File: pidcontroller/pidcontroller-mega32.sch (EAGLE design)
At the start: 19 parts, among them IC2 MAX3232CWE, IC3 MEGA32-A

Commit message: more work!
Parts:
- SV3: device con-lstb:MA03-2 -> con-lstb:MA06-1
- renumbered SSR2- to PUMP
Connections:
- removed net LCDCONTR: R3.S, SV1.3
- removed net N$21: IC3.(OC1A)PD5, OW-TMP.P
- new net N$17: R3.S, SV1.2
- net GND: now also IC3.GND, IC3.GND1, IC3.GND2, SV1.1, SV3.5; no longer IC3.VCC2, SV1.2, SV3.6
- net N$10: now also IC3.(OC2)PD7; no longer IC3.(TOSC2)PC7
- net N$14: now also IC3.(MOSI)PB5; no longer IC3.(MISO)PB6
- net N$15: now also IC3.(MISO)PB6, SV3.2; no longer IC3.(MOSI)PB5, SV3.4
- net N$4: now also IC3.(OC1A)PD5; no longer IC3.(TOSC1)PC6
- net RESET: now also SV3.4; no longer SV3.5
- net VCC: now also IC3.AVCC, IC3.VCC1, IC3.VCC2, SV1.3, SV3.6; no longer SV1.1, SV3.2
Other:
- moved on the sheet: OW-TMP, SV3

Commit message: prettified board
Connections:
- net GND: now also SV3.6; no longer SV3.5
- net VCC: now also SV3.5; no longer SV3.6
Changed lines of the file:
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@@
-</segment>
-<segment>
-<pinref part="P+4" gate="VCC" pin="VCC"/>
-<wire x1="99.06" y1="63.5" x2="96.52" y2="63.5" width="0.1524" layer="91"/>
-<pinref part="SV3" gate="1" pin="6"/>
-<wire x1="96.52" y1="63.5" x2="96.52" y2="48.26" width="0.1524" layer="91"/>
-<wire x1="96.52" y1="48.26" x2="104.14" y2="48.26" width="0.1524" layer="91"/>
 </segment>
 <segment>
@@
 <wire x1="96.52" y1="101.6" x2="96.52" y2="88.9" width="0.1524" layer="91"/>
 <wire x1="96.52" y1="88.9" x2="104.14" y2="88.9" width="0.1524" layer="91"/>
+</segment>
+<segment>
+<pinref part="P+4" gate="VCC" pin="VCC"/>
+<pinref part="SV3" gate="1" pin="5"/>
+<wire x1="99.06" y1="63.5" x2="99.06" y2="50.8" width="0.1524" layer="91"/>
+<wire x1="99.06" y1="50.8" x2="104.14" y2="50.8" width="0.1524" layer="91"/>
 </segment>
 </net>
@@
 </segment>
 <segment>
-<pinref part="GND6" gate="1" pin="GND"/>
-<pinref part="SV3" gate="1" pin="5"/>
-<wire x1="99.06" y1="43.18" x2="99.06" y2="50.8" width="0.1524" layer="91"/>
-<wire x1="99.06" y1="50.8" x2="104.14" y2="50.8" width="0.1524" layer="91"/>
-</segment>
-<segment>
 <pinref part="SV1" gate="1" pin="1"/>
 <pinref part="GND5" gate="1" pin="GND"/>
@@
 <wire x1="86.36" y1="93.98" x2="86.36" y2="101.6" width="0.1524" layer="91"/>
 </segment>
+<segment>
+<pinref part="GND6" gate="1" pin="GND"/>
+<pinref part="SV3" gate="1" pin="6"/>
+<wire x1="99.06" y1="43.18" x2="99.06" y2="48.26" width="0.1524" layer="91"/>
+<wire x1="99.06" y1="48.26" x2="104.14" y2="48.26" width="0.1524" layer="91"/>
+</segment>
 </net>

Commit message: updated schematic and board
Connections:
- new net N$16: IC3.(AIN1/OC0)PB3, OW-TMP.P
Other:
- moved on the sheet: OW-TMP
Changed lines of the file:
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@@
 <instance part="P+11" gate="VCC" x="48.26" y="93.98" rot="R180"/>
 <instance part="GND9" gate="1" x="48.26" y="114.3" rot="R180"/>
-<instance part="OW-TMP" gate="1" x="93.98" y="25.4" rot="R90"/>
+<instance part="OW-TMP" gate="1" x="66.04" y="55.88" rot="R180"/>
 <instance part="IC3" gate="G$1" x="27.94" y="45.72"/>
 <instance part="5VIN" gate="G$1" x="-40.64" y="71.12"/>
@@
 </segment>
 </net>
+<net name="N$16" class="0">
+<segment>
+<pinref part="IC3" gate="G$1" pin="(AIN1/OC0)PB3"/>
+<pinref part="OW-TMP" gate="1" pin="P"/>
+<wire x1="48.26" y1="55.88" x2="63.5" y2="55.88" width="0.1524" layer="91"/>
+</segment>
+</net>

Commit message: updated board for PID
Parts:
- added ISP: (no value), pinhead:PINHD-2X3
- added JP2, JP3, JP4, JP5, JP6, JP7: (no value), pinhead:PINHD-1X1
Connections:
- new net N$21: ISP.6, JP2.1
- new net N$22: ISP.4, JP3.1
- new net N$25: ISP.2, JP4.1
- new net N$26: ISP.1, JP7.1
- new net N$27: ISP.3, JP6.1
- new net N$28: ISP.5, JP5.1
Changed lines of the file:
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@@
 <?xml version="1.0" encoding="utf-8"?>
 <!DOCTYPE eagle SYSTEM "eagle.dtd">
-<eagle version="6.6.0">
+<eagle version="6.4">
 <drawing>
 <settings>
@@
 <part name="P+4" library="supply1" deviceset="VCC" device=""/>
 <part name="GND6" library="supply1" deviceset="GND" device=""/>
+<part name="ISP" library="pinhead" deviceset="PINHD-2X3" device=""/>
+<part name="JP2" library="pinhead" deviceset="PINHD-1X1" device=""/>
+<part name="JP3" library="pinhead" deviceset="PINHD-1X1" device=""/>
+<part name="JP4" library="pinhead" deviceset="PINHD-1X1" device=""/>
+<part name="JP5" library="pinhead" deviceset="PINHD-1X1" device=""/>
+<part name="JP6" library="pinhead" deviceset="PINHD-1X1" device=""/>
+<part name="JP7" library="pinhead" deviceset="PINHD-1X1" device=""/>
 </parts>
 <sheets>
@@
 <instance part="P+4" gate="VCC" x="99.06" y="66.04"/>
 <instance part="GND6" gate="1" x="99.06" y="40.64"/>
+<instance part="ISP" gate="A" x="154.94" y="99.06" rot="R180"/>
+<instance part="JP2" gate="G$1" x="134.62" y="109.22" rot="R90"/>
+<instance part="JP3" gate="G$1" x="134.62" y="99.06" rot="R90"/>
+<instance part="JP4" gate="G$1" x="134.62" y="86.36" rot="R90"/>
+<instance part="JP5" gate="G$1" x="175.26" y="114.3" rot="R90"/>
+<instance part="JP6" gate="G$1" x="175.26" y="101.6" rot="R90"/>
+<instance part="JP7" gate="G$1" x="175.26" y="88.9" rot="R90"/>
 </instances>
 <busses>
@@
 </segment>
 </net>
+<net name="N$22" class="0">
+<segment>
+<pinref part="JP3" gate="G$1" pin="1"/>
+<wire x1="134.62" y1="96.52" x2="144.78" y2="96.52" width="0.1524" layer="91"/>
+<wire x1="144.78" y1="96.52" x2="144.78" y2="99.06" width="0.1524" layer="91"/>
+<pinref part="ISP" gate="A" pin="4"/>
+<wire x1="144.78" y1="99.06" x2="149.86" y2="99.06" width="0.1524" layer="91"/>
+</segment>
+</net>
+<net name="N$25" class="0">
+<segment>
+<pinref part="JP4" gate="G$1" pin="1"/>
+<wire x1="134.62" y1="83.82" x2="147.32" y2="83.82" width="0.1524" layer="91"/>
+<wire x1="147.32" y1="83.82" x2="147.32" y2="96.52" width="0.1524" layer="91"/>
+<pinref part="ISP" gate="A" pin="2"/>
+<wire x1="147.32" y1="96.52" x2="149.86" y2="96.52" width="0.1524" layer="91"/>
+</segment>
+</net>
+<net name="N$26" class="0">
+<segment>
+<pinref part="JP7" gate="G$1" pin="1"/>
+<wire x1="175.26" y1="86.36" x2="162.56" y2="86.36" width="0.1524" layer="91"/>
+<wire x1="162.56" y1="86.36" x2="162.56" y2="96.52" width="0.1524" layer="91"/>
+<pinref part="ISP" gate="A" pin="1"/>
+<wire x1="162.56" y1="96.52" x2="157.48" y2="96.52" width="0.1524" layer="91"/>
+</segment>
+</net>
+<net name="N$27" class="0">
+<segment>
+<pinref part="JP6" gate="G$1" pin="1"/>
+<pinref part="ISP" gate="A" pin="3"/>
+<wire x1="175.26" y1="99.06" x2="157.48" y2="99.06" width="0.1524" layer="91"/>
+</segment>
+</net>
+<net name="N$28" class="0">
+<segment>
+<pinref part="JP5" gate="G$1" pin="1"/>
+<wire x1="175.26" y1="111.76" x2="162.56" y2="111.76" width="0.1524" layer="91"/>
+<wire x1="162.56" y1="111.76" x2="162.56" y2="101.6" width="0.1524" layer="91"/>
+<pinref part="ISP" gate="A" pin="5"/>
+<wire x1="162.56" y1="101.6" x2="157.48" y2="101.6" width="0.1524" layer="91"/>
+</segment>
+</net>
+<net name="N$21" class="0">
+<segment>
+<pinref part="ISP" gate="A" pin="6"/>
+<wire x1="149.86" y1="101.6" x2="144.78" y2="101.6" width="0.1524" layer="91"/>
+<wire x1="144.78" y1="101.6" x2="144.78" y2="106.68" width="0.1524" layer="91"/>
+<pinref part="JP2" gate="G$1" pin="1"/>
+<wire x1="144.78" y1="106.68" x2="134.62" y2="106.68" width="0.1524" layer="91"/>
+</segment>
+</net>

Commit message: updated board
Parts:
- added BTNDN, BTNOK, BTNUP: (no value), wirepad:2,15/1,0
- added R4, R5, R6: (no value), resistor:R-EU_R0603
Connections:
- new net BTNDN: BTNDN.P, IC3.(INT1)PD3, R5.1
- new net BTNOK: BTNOK.P, IC3.(INT0)PD2, R6.1
- new net BTNUP: BTNUP.P, IC3.(OC1B)PD4, R4.1
- net GND: now also R4.2, R5.2, R6.2
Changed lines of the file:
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@@
 <?xml version="1.0" encoding="utf-8"?>
 <!DOCTYPE eagle SYSTEM "eagle.dtd">
-<eagle version="6.4">
+<eagle version="6.5.0">
 <drawing>
 <settings>
@@
 <part name="JP6" library="pinhead" deviceset="PINHD-1X1" device=""/>
 <part name="JP7" library="pinhead" deviceset="PINHD-1X1" device=""/>
+<part name="GND8" library="supply1" deviceset="GND" device=""/>
+<part name="BTNUP" library="wirepad" deviceset="2,15/1,0" device=""/>
+<part name="BTNDN" library="wirepad" deviceset="2,15/1,0" device=""/>
+<part name="BTNOK" library="wirepad" deviceset="2,15/1,0" device=""/>
+<part name="R4" library="resistor" deviceset="R-EU_" device="R0603"/>
+<part name="R5" library="resistor" deviceset="R-EU_" device="R0603"/>
+<part name="R6" library="resistor" deviceset="R-EU_" device="R0603"/>
 </parts>
 <sheets>
@@
 <instance part="JP6" gate="G$1" x="175.26" y="101.6" rot="R90"/>
 <instance part="JP7" gate="G$1" x="175.26" y="88.9" rot="R90"/>
+<instance part="GND8" gate="1" x="185.42" y="35.56"/>
+<instance part="BTNUP" gate="1" x="208.28" y="66.04" rot="R180"/>
+<instance part="BTNDN" gate="1" x="208.28" y="55.88" rot="R180"/>
+<instance part="BTNOK" gate="1" x="208.28" y="45.72" rot="R180"/>
+<instance part="R4" gate="G$1" x="190.5" y="66.04" rot="R180"/>
+<instance part="R5" gate="G$1" x="190.5" y="55.88" rot="R180"/>
+<instance part="R6" gate="G$1" x="190.5" y="45.72" rot="R180"/>
 </instances>
 <busses>
@@
 <wire x1="99.06" y1="48.26" x2="104.14" y2="48.26" width="0.1524" layer="91"/>
 </segment>
+<segment>
+<pinref part="GND8" gate="1" pin="GND"/>
+<pinref part="R6" gate="G$1" pin="2"/>
+<wire x1="185.42" y1="38.1" x2="185.42" y2="45.72" width="0.1524" layer="91"/>
+<pinref part="R5" gate="G$1" pin="2"/>
+<wire x1="185.42" y1="45.72" x2="185.42" y2="55.88" width="0.1524" layer="91"/>
+<junction x="185.42" y="45.72"/>
+<pinref part="R4" gate="G$1" pin="2"/>
+<wire x1="185.42" y1="55.88" x2="185.42" y2="66.04" width="0.1524" layer="91"/>
+<junction x="185.42" y="55.88"/>
+</segment>
 </net>
 <net name="RESET" class="0">
@@
 </segment>
 </net>
+<net name="BTNUP" class="0">
+<segment>
+<pinref part="R4" gate="G$1" pin="1"/>
+<pinref part="BTNUP" gate="1" pin="P"/>
+<wire x1="195.58" y1="66.04" x2="205.74" y2="66.04" width="0.1524" layer="91"/>
+</segment>
+<segment>
+<pinref part="IC3" gate="G$1" pin="(OC1B)PD4"/>
+<wire x1="48.26" y1="12.7" x2="53.34" y2="12.7" width="0.1524" layer="91"/>
+</segment>
+</net>
+<net name="BTNDN" class="0">
+<segment>
+<pinref part="R5" gate="G$1" pin="1"/>
+<pinref part="BTNDN" gate="1" pin="P"/>
+<wire x1="195.58" y1="55.88" x2="205.74" y2="55.88" width="0.1524" layer="91"/>
+</segment>
+<segment>
+<pinref part="IC3" gate="G$1" pin="(INT1)PD3"/>
+<wire x1="48.26" y1="10.16" x2="53.34" y2="10.16" width="0.1524" layer="91"/>
+</segment>
+</net>
+<net name="BTNOK" class="0">
+<segment>
+<pinref part="R6" gate="G$1" pin="1"/>
+<pinref part="BTNOK" gate="1" pin="P"/>
+<wire x1="195.58" y1="45.72" x2="205.74" y2="45.72" width="0.1524" layer="91"/>
+</segment>
+<segment>
+<pinref part="IC3" gate="G$1" pin="(INT0)PD2"/>
+<wire x1="48.26" y1="7.62" x2="53.34" y2="7.62" width="0.1524" layer="91"/>
+</segment>
+</net>

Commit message: updated isp
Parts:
- removed JP2, JP4: (no value), pinhead:PINHD-1X1
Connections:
- removed net N$21: ISP.6, JP2.1
- removed net N$25: ISP.2, JP4.1
- net GND: now also ISP.6
- net VCC: now also ISP.2
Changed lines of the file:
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@@
 <part name="GND6" library="supply1" deviceset="GND" device=""/>
 <part name="ISP" library="pinhead" deviceset="PINHD-2X3" device=""/>
-<part name="JP2" library="pinhead" deviceset="PINHD-1X1" device=""/>
 <part name="JP3" library="pinhead" deviceset="PINHD-1X1" device=""/>
-<part name="JP4" library="pinhead" deviceset="PINHD-1X1" device=""/>
 <part name="JP5" library="pinhead" deviceset="PINHD-1X1" device=""/>
 <part name="JP6" library="pinhead" deviceset="PINHD-1X1" device=""/>
@@
 <part name="R5" library="resistor" deviceset="R-EU_" device="R0603"/>
 <part name="R6" library="resistor" deviceset="R-EU_" device="R0603"/>
+<part name="GND10" library="supply1" deviceset="GND" device=""/>
+<part name="P+6" library="supply1" deviceset="VCC" device=""/>
 </parts>
 <sheets>
@@
 <instance part="GND6" gate="1" x="99.06" y="40.64"/>
 <instance part="ISP" gate="A" x="154.94" y="99.06" rot="R180"/>
-<instance part="JP2" gate="G$1" x="134.62" y="109.22" rot="R90"/>
 <instance part="JP3" gate="G$1" x="134.62" y="99.06" rot="R90"/>
-<instance part="JP4" gate="G$1" x="134.62" y="86.36" rot="R90"/>
 <instance part="JP5" gate="G$1" x="175.26" y="114.3" rot="R90"/>
 <instance part="JP6" gate="G$1" x="175.26" y="101.6" rot="R90"/>
@@
 <instance part="R5" gate="G$1" x="190.5" y="55.88" rot="R180"/>
 <instance part="R6" gate="G$1" x="190.5" y="45.72" rot="R180"/>
+<instance part="GND10" gate="1" x="134.62" y="111.76" rot="R180"/>
+<instance part="P+6" gate="VCC" x="134.62" y="76.2" rot="R180"/>
 </instances>
 <busses>
@@
 <wire x1="99.06" y1="50.8" x2="104.14" y2="50.8" width="0.1524" layer="91"/>
 </segment>
+<segment>
+<wire x1="134.62" y1="83.82" x2="147.32" y2="83.82" width="0.1524" layer="91"/>
+<wire x1="147.32" y1="83.82" x2="147.32" y2="96.52" width="0.1524" layer="91"/>
+<pinref part="ISP" gate="A" pin="2"/>
+<wire x1="147.32" y1="96.52" x2="149.86" y2="96.52" width="0.1524" layer="91"/>
+<pinref part="P+6" gate="VCC" pin="VCC"/>
+<wire x1="134.62" y1="83.82" x2="134.62" y2="78.74" width="0.1524" layer="91"/>
+</segment>
 </net>
 <net name="N$9" class="0">
@@
 <junction x="185.42" y="55.88"/>
 </segment>
+<segment>
+<pinref part="ISP" gate="A" pin="6"/>
+<wire x1="149.86" y1="101.6" x2="144.78" y2="101.6" width="0.1524" layer="91"/>
+<wire x1="144.78" y1="101.6" x2="144.78" y2="106.68" width="0.1524" layer="91"/>
+<wire x1="144.78" y1="106.68" x2="134.62" y2="106.68" width="0.1524" layer="91"/>
+<pinref part="GND10" gate="1" pin="GND"/>
+<wire x1="134.62" y1="106.68" x2="134.62" y2="109.22" width="0.1524" layer="91"/>
+</segment>
 </net>
 <net name="RESET" class="0">
@@
 </segment>
 </net>
-<net name="N$25" class="0">
-<segment>
-<pinref part="JP4" gate="G$1" pin="1"/>
-<wire x1="134.62" y1="83.82" x2="147.32" y2="83.82" width="0.1524" layer="91"/>
-<wire x1="147.32" y1="83.82" x2="147.32" y2="96.52" width="0.1524" layer="91"/>
-<pinref part="ISP" gate="A" pin="2"/>
-<wire x1="147.32" y1="96.52" x2="149.86" y2="96.52" width="0.1524" layer="91"/>
-</segment>
-</net>
 <net name="N$26" class="0">
 <segment>
@@
 </segment>
 </net>
-<net name="N$21" class="0">
-<segment>
-<pinref part="ISP" gate="A" pin="6"/>
-<wire x1="149.86" y1="101.6" x2="144.78" y2="101.6" width="0.1524" layer="91"/>
-<wire x1="144.78" y1="101.6" x2="144.78" y2="106.68" width="0.1524" layer="91"/>
-<pinref part="JP2" gate="G$1" pin="1"/>
-<wire x1="144.78" y1="106.68" x2="134.62" y2="106.68" width="0.1524" layer="91"/>
-</segment>
-</net>

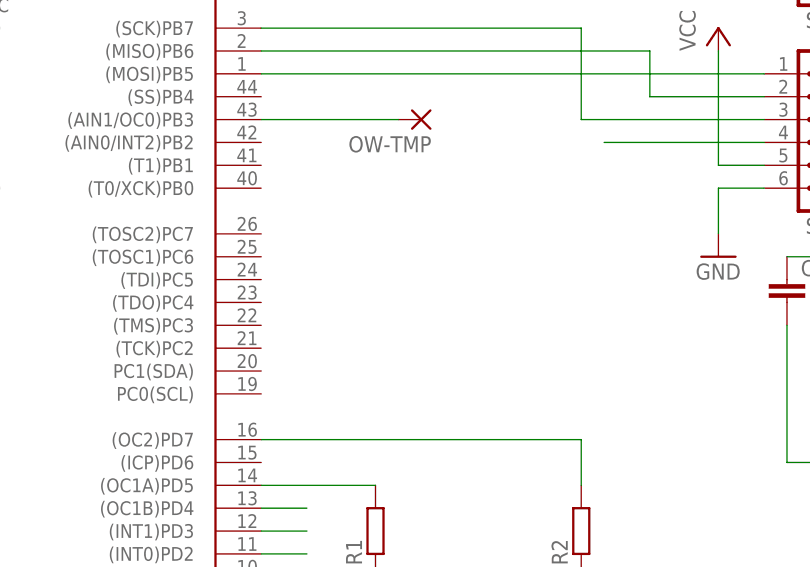
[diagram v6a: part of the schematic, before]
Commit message: added extra pins
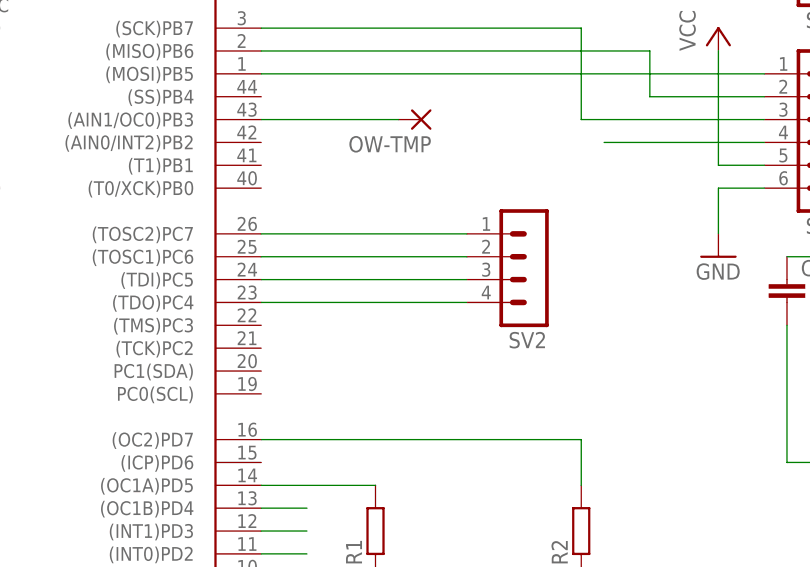
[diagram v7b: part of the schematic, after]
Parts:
- added SV2: (no value), con-lstb:MA04-1
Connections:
- new net N$40: IC3.(TOSC2)PC7, SV2.1
- new net N$41: IC3.(TOSC1)PC6, SV2.2
- new net N$42: IC3.(TDI)PC5, SV2.3
- new net N$43: IC3.(TDO)PC4, SV2.4
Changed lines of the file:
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@@
 <part name="GND10" library="supply1" deviceset="GND" device=""/>
 <part name="P+6" library="supply1" deviceset="VCC" device=""/>
+<part name="SV2" library="con-lstb" deviceset="MA04-1" device=""/>
 </parts>
 <sheets>
@@
 <instance part="GND10" gate="1" x="134.62" y="111.76" rot="R180"/>
 <instance part="P+6" gate="VCC" x="134.62" y="76.2" rot="R180"/>
+<instance part="SV2" gate="1" x="78.74" y="38.1" rot="R180"/>
 </instances>
 <busses>
@@
 </segment>
 </net>
+<net name="N$40" class="0">
+<segment>
+<pinref part="IC3" gate="G$1" pin="(TOSC2)PC7"/>
+<pinref part="SV2" gate="1" pin="1"/>
+<wire x1="48.26" y1="43.18" x2="71.12" y2="43.18" width="0.1524" layer="91"/>
+</segment>
+</net>
+<net name="N$42" class="0">
+<segment>
+<pinref part="IC3" gate="G$1" pin="(TDI)PC5"/>
+<pinref part="SV2" gate="1" pin="3"/>
+<wire x1="48.26" y1="38.1" x2="71.12" y2="38.1" width="0.1524" layer="91"/>
+</segment>
+</net>
+<net name="N$43" class="0">
+<segment>
+<pinref part="IC3" gate="G$1" pin="(TDO)PC4"/>
+<pinref part="SV2" gate="1" pin="4"/>
+<wire x1="48.26" y1="35.56" x2="71.12" y2="35.56" width="0.1524" layer="91"/>
+</segment>
+</net>
+<net name="N$41" class="0">
+<segment>
+<pinref part="SV2" gate="1" pin="2"/>
+<pinref part="IC3" gate="G$1" pin="(TOSC1)PC6"/>
+<wire x1="71.12" y1="40.64" x2="48.26" y2="40.64" width="0.1524" layer="91"/>
+</segment>
+</net>
